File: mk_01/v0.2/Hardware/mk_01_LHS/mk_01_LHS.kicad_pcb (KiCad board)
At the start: 2 copper layers, 165.1 x 102.9 mm, 80 parts, among them SW1 SW_Push_Dual, U1 nice_nano

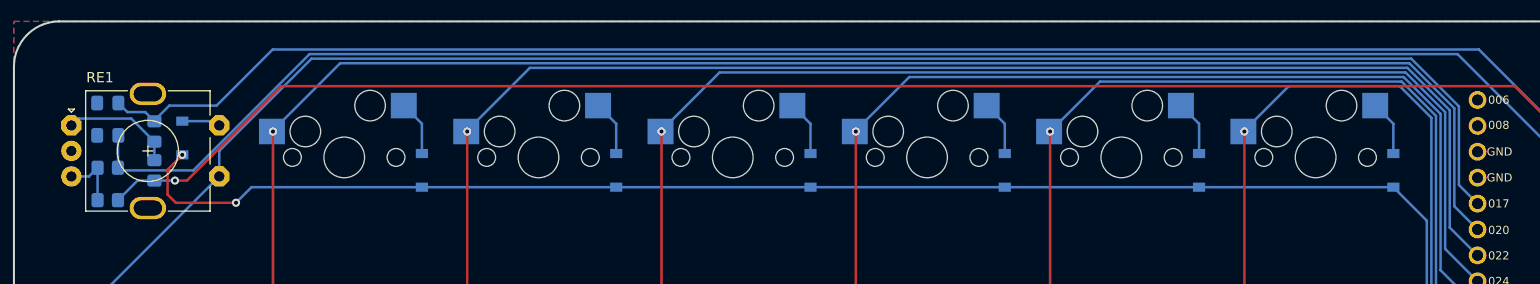
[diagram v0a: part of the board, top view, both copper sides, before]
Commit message: Right hand side mostly completed
The right hand side of the keyboard is pretty much complete, and after a final checkover of everything I think it's ready for production. I'm going to clean up the left hand side board design and schematic to match the right hand schematic style, since I based the left hand side on v0.1, and the right hand side was done from scratch.
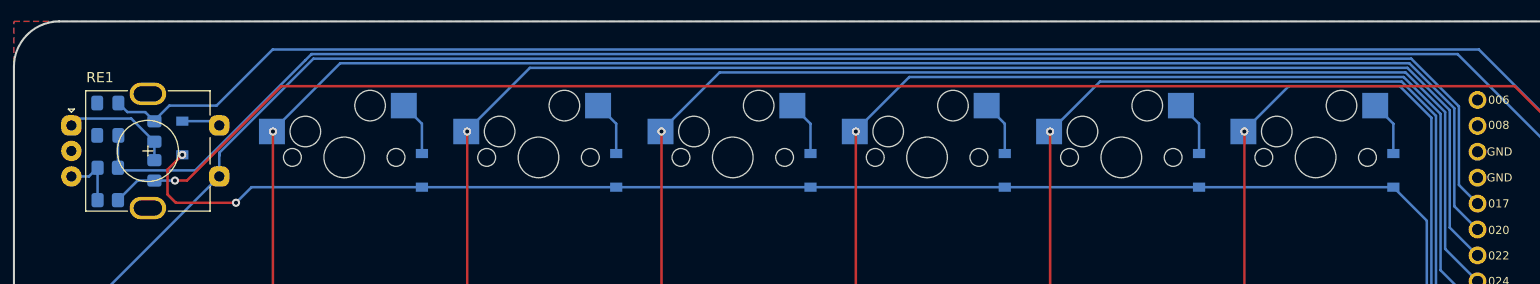
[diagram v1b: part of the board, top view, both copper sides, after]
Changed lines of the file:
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@@
     (fp_line (start 13.5 8.3) (end 1.5 8.3) (layer "F.Fab") (width 0.12))
     (fp_circle (center 7.5 2.5) (end 10.5 2.5) (layer "F.Fab") (width 0.12) (fill none))
-    (pad "A" thru_hole roundrect (at 0 0) (size 2 2) (drill 1) (layers *.Cu *.Mask) (roundrect_rratio 0)
-      (chamfer_ratio 0.3) (chamfer top_left top_right bottom_left bottom_right)
+    (pad "A" thru_hole roundrect (at 0 0) (size 2 2) (drill 1) (layers *.Cu *.Mask) (roundrect_rratio 0.35)
       (net 4 "Net-(R1-Pad2)") (pinfunction "A") (pintype "passive"))
     (pad "B" thru_hole circle (at 0 5) (size 2 2) (drill 1) (layers *.Cu *.Mask)
@@
     (pad "MP" thru_hole oval (at 7.5 8.1) (size 3.6 2.2) (drill oval 2.8 1.5) (layers *.Cu *.Mask))
     (pad "MP" thru_hole oval (at 7.5 -3.1) (size 3.6 2.2) (drill oval 2.8 1.5) (layers *.Cu *.Mask))
-    (pad "S1" thru_hole roundrect (at 14.5 5) (size 2 2) (drill 1) (layers *.Cu *.Mask) (roundrect_rratio 0)
-      (chamfer_ratio 0.3) (chamfer top_left top_right bottom_left bottom_right)
+    (pad "S1" thru_hole roundrect (at 14.5 5) (size 2 2) (drill 1) (layers *.Cu *.Mask) (roundrect_rratio 0.35)
       (net 23 "col0") (pinfunction "S1") (pintype "passive"))
-    (pad "S2" thru_hole roundrect (at 14.5 0) (size 2 2) (drill 1) (layers *.Cu *.Mask) (roundrect_rratio 0)
-      (chamfer_ratio 0.3) (chamfer top_left top_right bottom_left bottom_right)
+    (pad "S2" thru_hole roundrect (at 14.5 0) (size 2 2) (drill 1) (layers *.Cu *.Mask) (roundrect_rratio 0.35)
       (net 63 "Net-(RE1-PadS2)") (pinfunction "S2") (pintype "passive"))
     (model "${KICAD6_3DMODEL_DIR}/Rotary_Encoder.3dshapes/RotaryEncoder_Alps_EC11E-Switch_Vertical_H20mm.wrl"
@@
   (via (at 49.08 51.435) (size 0.8) (drill 0.4) (layers "F.Cu" "B.Cu") (net 12))
   (via (at 43.815 46.736) (size 0.8) (drill 0.4) (layers "F.Cu" "B.Cu") (net 12))
-  (segment (start 165.84192 53.19192) (end 165.84192 53.23308) (width 0.25) (layer "B.Cu") (net 12))
   (segment (start 49.08 51.435) (end 50.605 49.91) (width 0.25) (layer "B.Cu") (net 12))
   (segment (start 162.56 49.91) (end 162.94 49.91) (width 0.25) (layer "B.Cu") (net 12))
@@
   (segment (start 166.29144 43.10144) (end 166.29144 62.23319) (width 0.25) (layer "B.Cu") (net 22))
   (segment (start 147.855 44.45) (end 152.3 40.005) (width 0.25) (layer "B.Cu") (net 22))
+  (segment (start 56.672837 37.30788) (end 47.44 46.540717) (width 0.25) (layer "B.Cu") (net 23))
+  (segment (start 170.815 51.51675) (end 168.98856 49.69031) (width 0.25) (layer "B.Cu") (net 23))
+  (segment (start 168.98856 41.984253) (end 164.312187 37.30788) (width 0.25) (layer "B.Cu") (net 23))
+  (segment (start 47.44 46.540717) (end 47.44 46.805) (width 0.25) (layer "B.Cu") (net 23))
   (segment (start 33.555 63.5) (end 33.555 120.65) (width 0.25) (layer "B.Cu") (net 23))
-  (segment (start 47.44 48.855) (end 47.44 46.349658) (width 0.25) (layer "B.Cu") (net 23))
-  (segment (start 56.481778 37.30788) (end 164.312187 37.30788) (width 0.25) (layer "B.Cu") (net 23))
-  (segment (start 168.98856 41.984253) (end 168.98856 49.69031) (width 0.25) (layer "B.Cu") (net 23))
-  (segment (start 47.44 46.349658) (end 56.481778 37.30788) (width 0.25) (layer "B.Cu") (net 23))
-  (segment (start 168.98856 49.69031) (end 170.815 51.51675) (width 0.25) (layer "B.Cu") (net 23))
+  (segment (start 47.44 46.805) (end 47.44 46.54) (width 0.25) (layer "B.Cu") (net 23))
+  (segment (start 164.312187 37.30788) (end 56.672837 37.30788) (width 0.25) (layer "B.Cu") (net 23))
+  (segment (start 168.98856 49.69031) (end 168.98856 41.984253) (width 0.25) (layer "B.Cu") (net 23))
+  (segment (start 47.44 48.855) (end 47.44 46.805) (width 0.25) (layer "B.Cu") (net 23))
   (segment (start 33.555 63.5) (end 33.555 63.19) (width 0.25) (layer "B.Cu") (net 23))
   (segment (start 33.105 63.19) (end 47.44 48.855) (width 0.25) (layer "B.Cu") (net 23))
-  (segment (start 164.312187 37.30788) (end 168.98856 41.984253) (width 0.25) (layer "B.Cu") (net 23))
   (segment (start 179.705 74.295) (end 179.705 73.10675) (width 0.25) (layer "F.Cu") (net 24))
   (segment (start 179.705 73.10675) (end 186.055 66.75675) (width 0.25) (layer "F.Cu") (net 24))
@@
   (segment (start 41.079 43.45) (end 40.174 42.545) (width 0.25) (layer "B.Cu") (net 61))
   (segment (start 168.85661 36.85836) (end 186.055 54.05675) (width 0.25) (layer "B.Cu") (net 62))
-  (segment (start 37.761 48.26) (end 44.89394 48.26) (width 0.25) (layer "B.Cu") (net 62))
-  (segment (start 56.29558 36.85836) (end 168.85661 36.85836) (width 0.25) (layer "B.Cu") (net 62))
   (segment (start 37.507 44.8685) (end 37.5445 44.831) (width 0.25) (layer "B.Cu") (net 62))
   (segment (start 37.507 48.006) (end 37.507 44.8685) (width 0.25) (layer "B.Cu") (net 62))
-  (segment (start 44.89394 48.26) (end 56.29558 36.85836) (width 0.25) (layer "B.Cu") (net 62))
+  (segment (start 45.08389 48.26) (end 55.87889 37.465) (width 0.25) (layer "B.Cu") (net 62))
+  (segment (start 55.87889 37.465) (end 56.48553 36.85836) (width 0.25) (layer "B.Cu") (net 62))
+  (segment (start 56.54336 36.85836) (end 168.85661 36.85836) (width 0.25) (layer "B.Cu") (net 62))
+  (segment (start 37.761 48.26) (end 45.08389 48.26) (width 0.25) (layer "B.Cu") (net 62))
+  (segment (start 55.87889 37.465) (end 55.88 37.465) (width 0.25) (layer "B.Cu") (net 62))
   (segment (start 37.507 48.006) (end 37.761 48.26) (width 0.25) (layer "B.Cu") (net 62))
+  (segment (start 56.48553 36.85836) (end 56.54336 36.85836) (width 0.25) (layer "B.Cu") (net 62))
   (segment (start 46.92 43.335) (end 47.44 43.855) (width 0.25) (layer "F.Cu") (net 63))
   (segment (start 47.02 43.435) (end 47.44 43.855) (width 0.25) (layer "B.Cu") (net 63))
